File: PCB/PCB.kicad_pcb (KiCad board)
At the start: 2 copper layers, 2 parts

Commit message: schematic almost done
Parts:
- added C1: 100n, Capacitor_SMD:C_0603_1608Metric, F.Cu at (262.1, 79.7)
- added C2: 10u, Capacitor_SMD:C_0603_1608Metric, F.Cu at (277.5, 65.8)
- added C3: 100n, Capacitor_SMD:C_0603_1608Metric, F.Cu at (251.5, 94.5)
- added C4: 100n, Capacitor_SMD:C_0603_1608Metric, F.Cu at (255.6, 87.2)
- added C5: 100n, Capacitor_SMD:C_0603_1608Metric, F.Cu at (266.1, 78.1)
- added C6: 100n, Capacitor_SMD:C_0603_1608Metric, F.Cu at (261.5, 84.7)
- added D1: LED, LED_SMD:LED_0603_1608Metric, F.Cu at (235.3, 95.4)
- added D10: LED, LED_SMD:LED_0603_1608Metric, F.Cu at (243.5, 85.9)
- added D11: LED, LED_SMD:LED_0603_1608Metric, F.Cu at (243.5, 88.5)
- added D12: LED, LED_SMD:LED_0603_1608Metric, F.Cu at (223.5, 93.3)
- added D13: LED, LED_SMD:LED_0603_1608Metric, F.Cu at (223.2, 96.3)
- added D14: LED, LED_SMD:LED_0603_1608Metric, F.Cu at (231.3, 98.0)
- added D15: LED, LED_SMD:LED_0603_1608Metric, F.Cu at (253.5, 84.4)
- added D16: LED, LED_SMD:LED_0603_1608Metric, F.Cu at (231.3, 95.4)
- added D17: LED, LED_SMD:LED_0603_1608Metric, F.Cu at (258.1, 74.5)
- added D18: LED, LED_SMD:LED_0603_1608Metric, F.Cu at (247.5, 88.5)
- added D19: LED, LED_SMD:LED_0603_1608Metric, F.Cu at (243.5, 91.1)
- added D2: LED, LED_SMD:LED_0603_1608Metric, F.Cu at (231.6, 92.8)
- added D20: LED, LED_SMD:LED_0603_1608Metric, F.Cu at (258.1, 77.1)
- added D21: LED, LED_SMD:LED_0603_1608Metric, F.Cu at (219.1, 96.3)
- added D22: LED, LED_SMD:LED_0603_1608Metric, F.Cu at (227.5, 92.8)
- added D23: LED, LED_SMD:LED_0603_1608Metric, F.Cu at (273.5, 63.4)
- added D24: LED, LED_SMD:LED_0603_1608Metric, F.Cu at (239.4, 93.3)
- added D3: LED, LED_SMD:LED_0603_1608Metric, F.Cu at (247.5, 85.9)
- added D4: LED, LED_SMD:LED_0603_1608Metric, F.Cu at (235.3, 98.0)
- added D5: LED, LED_SMD:LED_0603_1608Metric, F.Cu at (243.4, 93.6)
- added D6: LED, LED_SMD:LED_0603_1608Metric, F.Cu at (269.5, 63.4)
- added D7: LED, LED_SMD:LED_0603_1608Metric, F.Cu at (269.5, 66.0)
- added D8: LED, LED_SMD:LED_0603_1608Metric, F.Cu at (264.8, 73.1)
- added D9: LED, LED_SMD:LED_0603_1608Metric, F.Cu at (227.2, 95.9)
- added J1: Conn_01x03, Connector_PinHeader_2.54mm:PinHeader_1x03_P2.54mm_Vertical, F.Cu at (253.8, 75.7)
- added J2: Conn_01x03_Male, Connector_PinHeader_2.54mm:PinHeader_1x03_P2.54mm_Vertical, F.Cu at (265.1, 64.4)
- added JP1: RST_JP, Jumper:SolderJumper-2_P1.3mm_Open_RoundedPad1.0x1.5mm, F.Cu at (219.2, 93.3)
- added R1: 1k, Resistor_SMD:R_0603_1608Metric, F.Cu at (277.5, 68.4)
- added R10: 1k, Resistor_SMD:R_0603_1608Metric, F.Cu at (269.4, 68.5)
- added R11: 1k, Resistor_SMD:R_0603_1608Metric, F.Cu at (259.6, 87.2)
- added R12: 1k, Resistor_SMD:R_0603_1608Metric, F.Cu at (266.2, 75.6)
- added R13: 1k, Resistor_SMD:R_0603_1608Metric, F.Cu at (239.3, 95.9)
- added R14: 1k, Resistor_SMD:R_0603_1608Metric, F.Cu at (270.2, 75.5)
- added R15: 1k, Resistor_SMD:R_0603_1608Metric, F.Cu at (273.5, 65.9)
- added R16: 1k, Resistor_SMD:R_0603_1608Metric, F.Cu at (273.5, 68.5)
- added R17: 1k, Resistor_SMD:R_0603_1608Metric, F.Cu at (247.5, 93.5)
- added R18: 1k, Resistor_SMD:R_0603_1608Metric, F.Cu at (251.5, 92.0)
- added R19: 1k, Resistor_SMD:R_0603_1608Metric, F.Cu at (262.1, 82.2)
- added R2: 1k, Resistor_SMD:R_0603_1608Metric, F.Cu at (247.5, 91.0)
- added R20: 1k, Resistor_SMD:R_0603_1608Metric, F.Cu at (258.1, 82.2)
- added R21: 1k, Resistor_SMD:R_0603_1608Metric, F.Cu at (262.1, 75.6)
- added R22: 1k, Resistor_SMD:R_0603_1608Metric, F.Cu at (257.5, 84.7)
- added R23: 1k, Resistor_SMD:R_0603_1608Metric, F.Cu at (251.5, 89.5)
- added R24: 1k, Resistor_SMD:R_0603_1608Metric, F.Cu at (277.5, 63.3)
- added R3: 1k, Resistor_SMD:R_0603_1608Metric, F.Cu at (258.1, 79.7)
- added R4: 1k, Resistor_SMD:R_0603_1608Metric, F.Cu at (268.8, 73.0)
- added R5: 1k, Resistor_SMD:R_0603_1608Metric, F.Cu at (243.3, 96.2)
- added R6: 1k, Resistor_SMD:R_0603_1608Metric, F.Cu at (272.9, 71.0)
- added R7: 1k, Resistor_SMD:R_0603_1608Metric, F.Cu at (255.6, 89.7)
- added R8: 1k, Resistor_SMD:R_0603_1608Metric, F.Cu at (251.5, 87.0)
- added R9: 1k, Resistor_SMD:R_0603_1608Metric, F.Cu at (247.3, 96.2)
- added U1: 74HC595D, xmasLib:SOIC127P600X175-16N, F.Cu at (247.5, 79.0)
- added U2: ATmega4809-A, Package_QFP:TQFP-48_7x7mm_P0.5mm, F.Cu at (249.2, 67.7)
- added U3: 74HC595D, xmasLib:SOIC127P600X175-16N, F.Cu at (237.5, 86.5)
- added U4: 74HC595D, xmasLib:SOIC127P600X175-16N, F.Cu at (258.9, 67.7)
- moved BT1 111.9 mm to (230.3, 71.5)
- moved BZ1 79.6 mm to (225.3, 86.2)
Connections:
- net GNDREF renamed GND
- BZ1 pad 1: unconnected-(BZ1-Pad1) -> /PA2
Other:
- board outline added: 150 x 100 mm

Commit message: Rough placement of components done
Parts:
- added J3: keys1_5, xmasLib:3w2b, F.Cu at (47.8, 111.2)
- added J4: keys6_12, xmasLib:4w3b, F.Cu at (82.8, 111.2)
- added J5: keys13_17, xmasLib:3w2b, F.Cu at (117.5, 111.2)
- added J6: keys18_24, xmasLib:4w3b, F.Cu at (152.5, 111.2)
- added SW1: PWR_SW, Button_Switch_SMD:SW_SPDT_CK-JS102011SAQN, F.Cu at (29.8, 41.1)
- J1: value Conn_01x03 -> Serial_3P
- J2: value Conn_01x03_Male -> UPDI_3P
- moved R1 241.9 mm to (37.0, 95.0)
- moved R4 216.0 mm to (53.4, 88.6)
- moved R3 210.7 mm to (48.0, 95.0)
- moved R6 207.4 mm to (66.8, 95.0)
- moved C1 206.1 mm to (56.0, 78.4), turned to -90 degrees
- moved D6 205.4 mm to (66.8, 96.7)
- moved R2 205.0 mm to (42.5, 88.6)
- moved D3 199.8 mm to (48.0, 96.7)
- moved D7 198.8 mm to (72.2, 90.3)
- moved D1 198.3 mm to (37.0, 96.7)
- moved BT1 191.2 mm to (39.2, 64.2), turned to 90 degrees
- moved D2 189.1 mm to (42.5, 90.3)
- moved D8 188.9 mm to (77.4, 96.7)
- moved D5 184.4 mm to (59.0, 96.7)
- moved R5 184.3 mm to (59.0, 95.0)
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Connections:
- BT1 pad 1: +3V0 -> Net-(BT1-Pad1)
- C2 pad 1: Net-(C2-Pad1) -> +3V0
- C3 pad 1: Net-(C2-Pad1) -> +3V0
- C4 pad 1: Net-(C2-Pad1) -> +3V0
- U2 pad 14: Net-(C2-Pad1) -> +3V0
- U2 pad 28: Net-(C2-Pad1) -> +3V0
- U2 pad 42: Net-(C2-Pad1) -> +3V0
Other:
- outline, holes or cut-outs redrawn

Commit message: Start routing
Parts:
- added J7: Conn_pen, Connector_PinHeader_2.54mm:PinHeader_1x01_P2.54mm_Vertical, F.Cu at (169.5, 32.5)
- added R25: ?, Resistor_SMD:R_0603_1608Metric, F.Cu at (170.0, 37.5)
- added SW2: SW_Push, Button_Switch_SMD:SW_Push_1P1T_NO_6x6mm_H9.5mm, F.Cu at (90.0, 35.0)
- J3, J5: footprint xmasLib:3w2b -> xmasLib:3w2bv2
- J4, J6: footprint xmasLib:4w3b -> xmasLib:4w3bv2
- moved C3 65.8 mm to (47.5, 52.5)
- moved J2 59.5 mm to (75.0, 35.0)
- moved J1 58.4 mm to (72.0, 35.0)
- moved BZ1 55.7 mm to (33.5, 55.0), turned to -90 degrees
- moved C2 55.1 mm to (59.2, 51.8)
- moved C4 51.7 mm to (63.5, 52.0)
- moved U2 51.1 mm to (52.5, 60.0)
- moved JP1 31.3 mm to (72.5, 50.0)
- moved BT1 30.1 mm to (52.0, 37.0), turned to 180 degrees
- moved U1 8.97 mm to (62.9, 71.5)
- moved D5 8.39 mm to (57.5, 88.4)
- moved R5 8.39 mm to (57.5, 86.8)
- moved C6 8.34 mm to (140.5, 69.5)
- moved C1 8.32 mm to (54.9, 70.1)
- moved C5 8.32 mm to (95.1, 69.6)
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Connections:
- J3 pad 1: unconnected-(J3-Pad1) -> /PC5
- J3 pad 2: unconnected-(J3-Pad2) -> /PC4
- J3 pad 3: unconnected-(J3-Pad3) -> /PC3
- J3 pad 4: unconnected-(J3-Pad4) -> /PC2
- J3 pad 5: unconnected-(J3-Pad5) -> /PC1
- J4 pad 1: unconnected-(J4-Pad1) -> /PC0
- J4 pad 2: unconnected-(J4-Pad2) -> /PB5
- J4 pad 3: unconnected-(J4-Pad3) -> /PB4
- J4 pad 4: unconnected-(J4-Pad4) -> /PB3
- J4 pad 5: unconnected-(J4-Pad5) -> /PB2
- J4 pad 6: unconnected-(J4-Pad6) -> /PB1
- J4 pad 7: unconnected-(J4-Pad7) -> /PB0
- J5 pad 1: unconnected-(J5-Pad1) -> /PF2
- J5 pad 2: unconnected-(J5-Pad2) -> /PF1
- J5 pad 3: unconnected-(J5-Pad3) -> /PF0
- J5 pad 4: unconnected-(J5-Pad4) -> /PE3
- J5 pad 5: unconnected-(J5-Pad5) -> /PE2
- J6 pad 1: unconnected-(J6-Pad1) -> /PE1
- J6 pad 2: unconnected-(J6-Pad2) -> /PE0
- J6 pad 3: unconnected-(J6-Pad3) -> /PD7
- J6 pad 4: unconnected-(J6-Pad4) -> /PD6
- J6 pad 5: unconnected-(J6-Pad5) -> /PD5
- J6 pad 6: unconnected-(J6-Pad6) -> /PD4
- J6 pad 7: unconnected-(J6-Pad7) -> /PD3
- U2 pad 10: unconnected-(U2-Pad10) -> /PC0
- U2 pad 11: unconnected-(U2-Pad11) -> /PC1
- U2 pad 12: unconnected-(U2-Pad12) -> /PC2
- U2 pad 13: unconnected-(U2-Pad13) -> /PC3
- U2 pad 16: unconnected-(U2-Pad16) -> /PC4
- U2 pad 17: unconnected-(U2-Pad17) -> /PC5
- U2 pad 18: unconnected-(U2-Pad18) -> /PC6
- U2 pad 19: unconnected-(U2-Pad19) -> /PC7
- U2 pad 20: unconnected-(U2-Pad20) -> /PD0
- U2 pad 21: unconnected-(U2-Pad21) -> /PD1
- U2 pad 22: unconnected-(U2-Pad22) -> /PD2
- U2 pad 23: unconnected-(U2-Pad23) -> /PD3
- U2 pad 24: unconnected-(U2-Pad24) -> /PD4
- U2 pad 25: unconnected-(U2-Pad25) -> /PD5
- U2 pad 26: unconnected-(U2-Pad26) -> /PD6
- U2 pad 27: unconnected-(U2-Pad27) -> /PD7
- U2 pad 30: unconnected-(U2-Pad30) -> /PE0
- U2 pad 31: unconnected-(U2-Pad31) -> /PE1
- U2 pad 32: unconnected-(U2-Pad32) -> /PE2
- U2 pad 33: unconnected-(U2-Pad33) -> /PE3
- U2 pad 34: unconnected-(U2-Pad34) -> /PF0
- U2 pad 35: unconnected-(U2-Pad35) -> /PF1
- U2 pad 36: unconnected-(U2-Pad36) -> /PF2
- U2 pad 4: unconnected-(U2-Pad4) -> /PB0
- U2 pad 5: unconnected-(U2-Pad5) -> /PB1
- U2 pad 6: unconnected-(U2-Pad6) -> /PB2
- U2 pad 7: unconnected-(U2-Pad7) -> /PB3
- U2 pad 8: unconnected-(U2-Pad8) -> /PB4
- U2 pad 9: unconnected-(U2-Pad9) -> /PB5
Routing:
- net /PF2: track 0.00 -> 280.0 mm
- net /PF1: track 0.00 -> 273.9 mm
- net /PE3: track 0.00 -> 259.5 mm
- net /PF0: track 0.00 -> 253.0 mm
- net /PE2: track 0.00 -> 245.9 mm
- net /PE1: track 0.00 -> 239.7 mm
- net /PE0: track 0.00 -> 233.4 mm
- net /PD6: track 0.00 -> 219.1 mm
- net /PD7: track 0.00 -> 212.4 mm
- net /PD5: track 0.00 -> 198.5 mm
- net /PD3: track 0.00 -> 184.6 mm
- net /PB0: track 0.00 -> 178.6 mm
- net /PB1: track 0.00 -> 172.5 mm
- net /PB3: track 0.00 -> 158.0 mm
- net /PB2: track 0.00 -> 151.7 mm
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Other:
- board text added: "Song List"

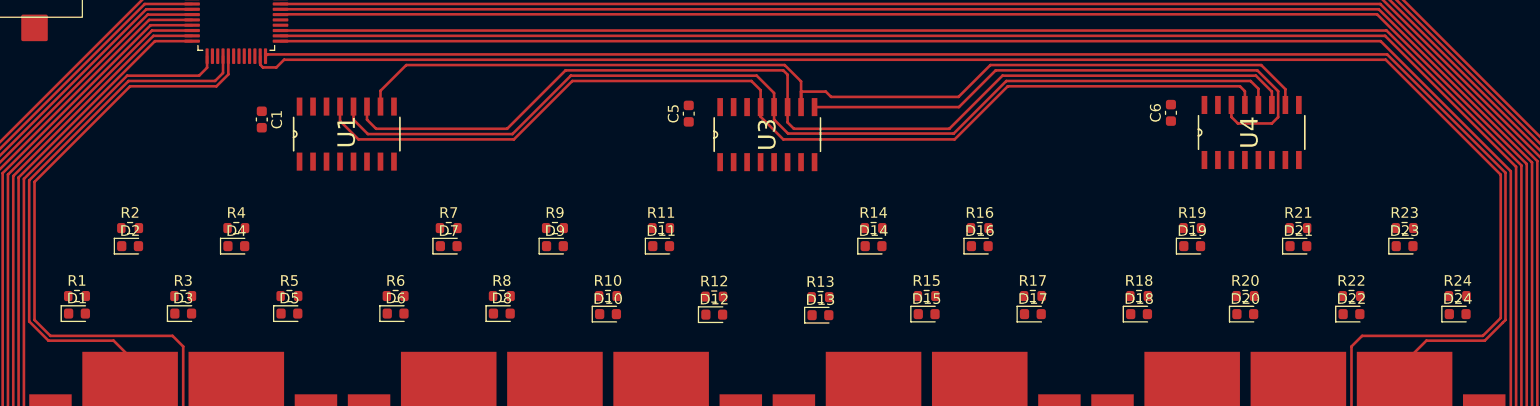
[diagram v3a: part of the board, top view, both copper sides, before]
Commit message: Routing of LEDS
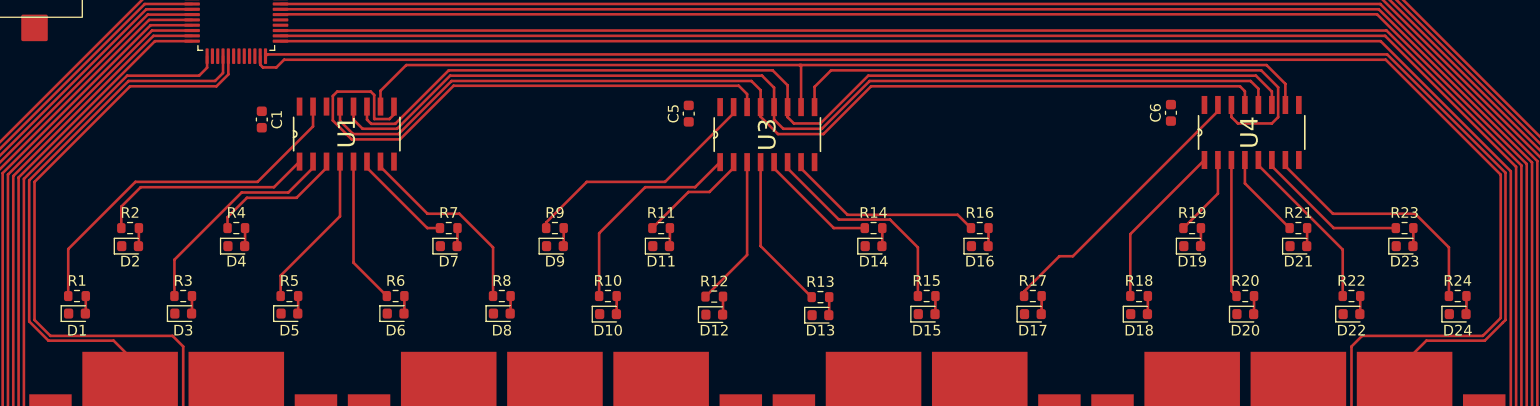
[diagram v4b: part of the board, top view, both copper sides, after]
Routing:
- net Net-(U1-Pad9): track 0.00 -> 54.9 mm
- net Net-(R1-Pad1): track 0.00 -> 34.1 mm
- net Net-(R17-Pad1): track 0.00 -> 26.3 mm
- net Net-(R24-Pad1): track 0.00 -> 23.7 mm
- net Net-(R9-Pad1): track 0.00 -> 23.0 mm
- net Net-(R3-Pad1): track 0.00 -> 20.6 mm
- net Net-(R2-Pad1): track 0.00 -> 20.6 mm
- net Net-(R15-Pad1): track 0.00 -> 20.5 mm
- net Net-(R10-Pad1): track 0.00 -> 20.1 mm
- net Net-(R16-Pad1): track 0.00 -> 18.9 mm
- net Net-(R8-Pad1): track 0.00 -> 18.8 mm
- net Net-(R22-Pad1): track 0.00 -> 16.1 mm
- net Net-(R18-Pad1): track 0.00 -> 15.7 mm
- net Net-(R5-Pad1): track 0.00 -> 15.0 mm
- net Net-(R13-Pad1): track 0.00 -> 14.7 mm
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
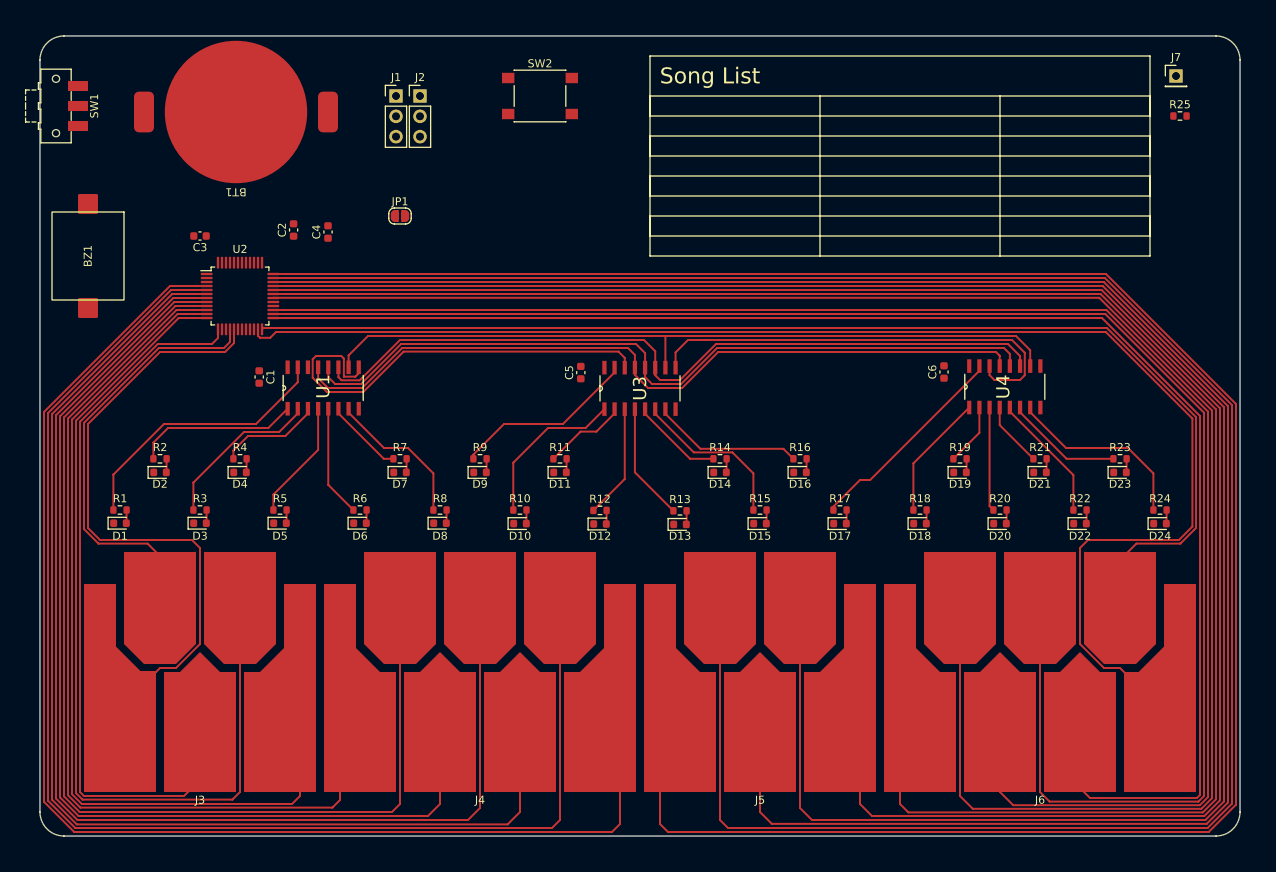
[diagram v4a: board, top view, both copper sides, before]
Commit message: Routing, pin assignments
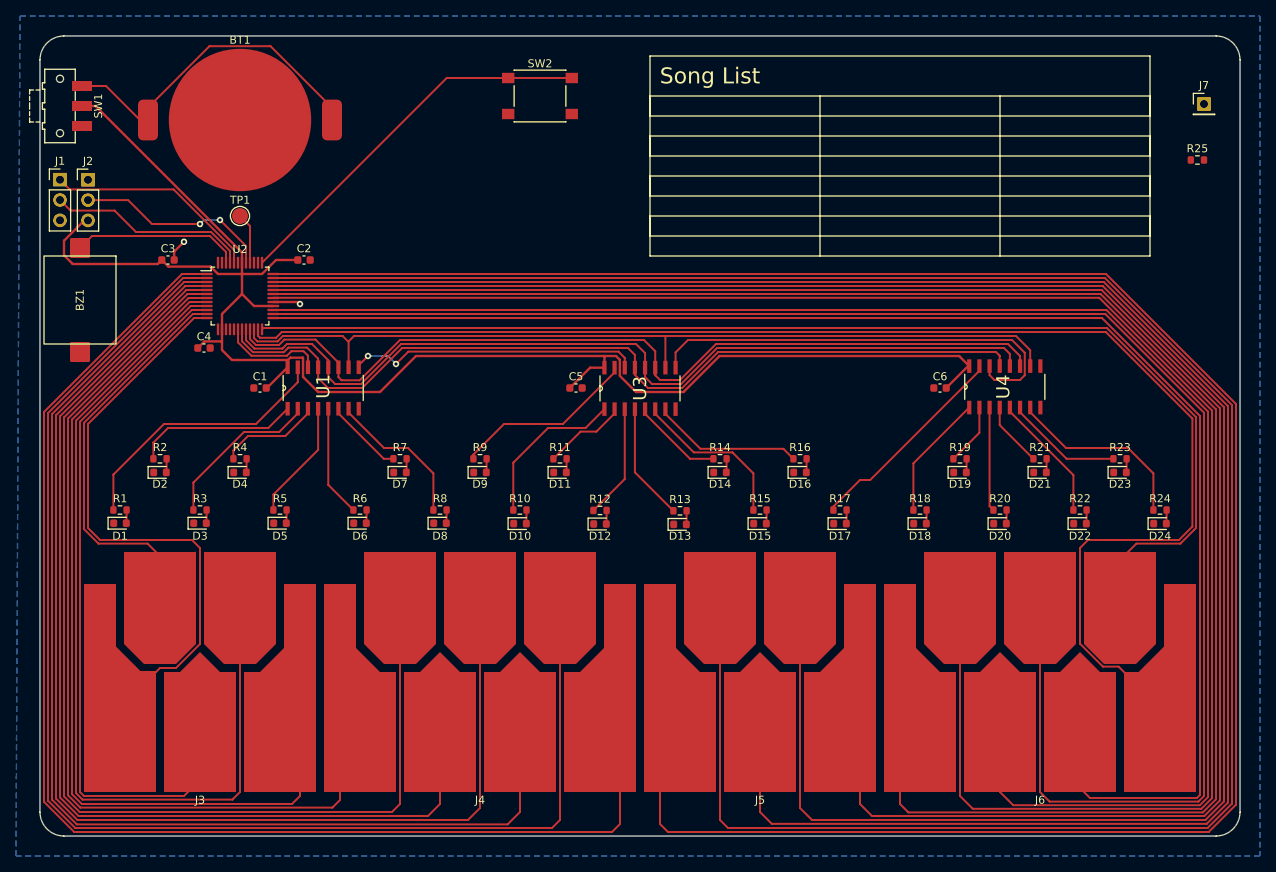
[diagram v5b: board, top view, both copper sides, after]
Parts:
- removed JP1: RST_JP, Jumper:SolderJumper-2_P1.3mm_Open_RoundedPad1.0x1.5mm
- added Ref**: Val**, xmasLib:Vectorized, B.Cu at (102.5, 77.5)
- added TP1: TestPoint, TestPoint:TestPoint_Pad_D2.0mm, F.Cu at (52.5, 50.0)
- R25: value ? -> 1K
- moved J1 43.3 mm to (30.0, 45.5)
- moved J2 42.8 mm to (33.5, 45.5)
- moved C4 21.2 mm to (48.0, 66.5), turned to 0 degrees
- moved R25 5.91 mm to (172.2, 43.0)
- moved BZ1 5.59 mm to (32.5, 60.5)
- moved C3 5.00 mm to (43.5, 55.5), turned to 0 degrees
- moved J7 4.95 mm to (173.0, 36.0)
- moved C2 3.97 mm to (60.5, 55.5), turned to 0 degrees
- moved C6 2.06 mm to (140.0, 71.5), turned to 0 degrees
- moved C5 2.02 mm to (94.5, 71.5), turned to 0 degrees
- moved C1 1.38 mm to (55.0, 71.5), turned to 0 degrees
- moved BT1 1.12 mm to (52.5, 38.0), turned to 0 degrees
- moved SW1 0.50 mm to (30.0, 36.2)
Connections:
- J3 pad 1: /PC5 -> /PC2
- J3 pad 2: /PC4 -> /PC1
- J3 pad 3: /PC3 -> /PC0
- J3 pad 4: /PC2 -> /PB5
- J3 pad 5: /PC1 -> /PB4
- J4 pad 1: /PC0 -> /PB3
- J4 pad 2: /PB5 -> /PB2
- J4 pad 3: /PB4 -> /PB1
- J4 pad 4: /PB3 -> /PB0
- J4 pad 5: /PB2 -> /PA7
- J4 pad 6: /PB1 -> /PA6
- J4 pad 7: /PB0 -> /PA5
- SW2 pad 1: unconnected-(SW2-Pad1) -> /SONG
- U1 pad 10: /~{RST} -> /PD2
- U1 pad 11: /SH_C -> /PD1
- U1 pad 12: /ST_C -> /PD0
- U1 pad 13: /~{OE} -> /PC7
- U1 pad 14: /SER -> /PC6
- U2 pad 1: unconnected-(U2-Pad1) -> /PA5
- U2 pad 13: /PC3 -> unconnected-(U2-Pad13)
- U2 pad 16: /PC4 -> unconnected-(U2-Pad16)
- U2 pad 17: /PC5 -> unconnected-(U2-Pad17)
- U2 pad 2: unconnected-(U2-Pad2) -> /PA6
- U2 pad 3: unconnected-(U2-Pad3) -> /PA7
- U2 pad 37: unconnected-(U2-Pad37) -> /SONG
- U3 pad 10: /~{RST} -> /PD2
- U3 pad 11: /SH_C -> /PD1
- U3 pad 12: /ST_C -> /PD0
- U3 pad 13: /~{OE} -> /PC7
- U4 pad 10: /~{RST} -> /PD2
- U4 pad 11: /SH_C -> /PD1
- U4 pad 12: /ST_C -> /PD0
- U4 pad 13: /~{OE} -> /PC7
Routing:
- net +3V0: track 0.00 -> 206.9 mm
- net /PA5: track 0.00 -> 179.2 mm
- net /PA6: track 0.00 -> 173.1 mm
- net /PA7: track 0.00 -> 152.3 mm
- net /PD1: track 0.00 -> 110.9 mm
- net /PD0: track 0.00 -> 110.4 mm
- net /PC7: track 0.00 -> 109.5 mm
- net /PD2: track 0.00 -> 109.1 mm
- net /PC3: track 98.5 -> 0.00 mm
- net /ST_C: track 96.4 -> 0.00 mm
- net /SH_C: track 96.3 -> 0.00 mm
- net /~{OE}: track 96.0 -> 0.00 mm
- net /~{RST}: track 94.5 -> 0.00 mm
- net /PC5: track 85.2 -> 0.00 mm
- net /PC1: track 123.5 -> 46.1 mm
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- added copper zone on B.Cu, net GND
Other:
- board text added: "Och Gott Nytt År"

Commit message: Final routing
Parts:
- removed J1: Serial_3P, Connector_PinHeader_2.54mm:PinHeader_1x03_P2.54mm_Vertical
- removed J2: UPDI_3P, Connector_PinHeader_2.54mm:PinHeader_1x03_P2.54mm_Vertical
- added J8: Conn_pen, MountingHole:MountingHole_2.2mm_M2_Pad_Via, F.Cu at (174.0, 31.0)
- added TP2: TestPoint_Small, TestPoint:TestPoint_Pad_D1.5mm, F.Cu at (35.6, 43.2)
- added TP3: TestPoint_Small, TestPoint:TestPoint_Pad_D1.5mm, F.Cu at (35.6, 45.7)
- added TP4: TestPoint_Small, TestPoint:TestPoint_Pad_D1.5mm, F.Cu at (33.0, 48.3)
- added TP5: TestPoint_Small, TestPoint:TestPoint_Pad_D1.5mm, F.Cu at (33.0, 43.2)
- added TP6: TestPoint_Small, TestPoint:TestPoint_Pad_D1.5mm, F.Cu at (33.0, 45.7)
- added TP7: TestPoint_Small, TestPoint:TestPoint_Pad_D1.5mm, F.Cu at (35.6, 48.3)
- J7: footprint Connector_PinHeader_2.54mm:PinHeader_1x01_P2.54mm_Vertical -> MountingHole:MountingHole_2.2mm_M2_Pad_Via
- TP1: value TestPoint -> Reset
- moved R25 2.36 mm to (174.0, 41.5), turned to 90 degrees
- moved J7 1.41 mm to (174.0, 37.0), turned to 90 degrees
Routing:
- net GND: track 6.22 -> 211.8 mm, vias 2 -> 26
- net Net-(J7-Pad1): track 0.00 -> 10.4 mm
- net +3V0: track 206.9 -> 196.7 mm
- net /PA1/RX: track 25.4 -> 23.3 mm
- net /PA0/TX: track 27.0 -> 24.9 mm
- net /UPDI: track 24.6 -> 23.1 mm
- net Net-(BT1-Pad1): track 42.5 -> 43.0 mm
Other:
- board text added: "+3V"
- board text added: "GND"
- board text added: "RESET"
- board text added: "RX"
- board text added: "TX"
- board text added: "UPDI"
